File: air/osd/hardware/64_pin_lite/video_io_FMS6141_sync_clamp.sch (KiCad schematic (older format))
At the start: 30 parts, among them U10 FMS6141, U11 DAC084S085, U12 ADG704, U13 OPA830, U8 MCP6562, U9 TLV3501

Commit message: osd tidying and added reset to header connector
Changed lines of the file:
@@
-EESchema Schematic File Version 2  date Sat 29 Nov 2014 10:43:44 GMT
+EESchema Schematic File Version 2  date Sun 30 Nov 2014 15:34:12 GMT
 LIBS:power
 LIBS:device
@@
 Sheet 8 8
 Title ""
-Date "29 nov 2014"
+Date "30 nov 2014"
 Rev ""
 Comp ""
@@
 	2200 4700 2200 4600
 Wire Wire Line
-	2550 2850 2550 2050
-Wire Wire Line
-	1300 2850 2550 2850
+	2550 2050 2550 2850
+Wire Wire Line
+	2550 2850 1300 2850
 Wire Wire Line
 	2550 1150 2550 950
@@
 	7250 6250 7250 5950
 Wire Wire Line
-	6650 6250 6650 5950
+	6650 5950 6650 6250
 Connection ~ 9600 6250
 Wire Wire Line
@@
 	2200 3600 2200 3500
 Wire Wire Line
-	3200 4500 4250 4500
+	4250 4500 3200 4500
 Wire Wire Line
 	8000 4500 4750 4500
@@
 Connection ~ 9900 1600
 Wire Wire Line
-	9900 2400 9900 1600
+	9900 1600 9900 2400
 Wire Wire Line
 	9900 2400 9600 2400
@@
 	8700 1600 8700 1500
 Wire Wire Line
-	8800 1700 8800 2400
+	8800 2400 8800 1700
 Wire Wire Line
 	1250 1600 1500 1600
@@
 	1550 6050 1550 5050
 Wire Wire Line
-	6250 1200 6650 1200
+	6650 1200 6250 1200
 Connection ~ 3950 7350
 Wire Wire Line
 	3950 7450 3950 7350
 Wire Wire Line
-	4200 7350 4200 7200
+	4200 7200 4200 7350
 Wire Wire Line
 	4200 7350 3650 7350
@@
 	4600 6550 3900 6550
 Wire Wire Line
-	3900 6200 3900 6550
+	3900 6550 3900 6200
 Wire Wire Line
 	1550 5050 5850 5050
@@
 	4800 1000 4800 1200
 Wire Wire Line
-	3300 700  6100 700
+	6100 700  3300 700
 Wire Wire Line
 	6650 1400 6400 1400
@@
 	7350 3700 8000 3700
 Wire Wire Line
-	1300 3100 3300 3100
+	3300 3100 1300 3100
 Wire Wire Line
 	6550 1600 6550 2050
@@
 	5850 5050 5850 2450
 Wire Wire Line
-	1300 6350 1850 6350
-Wire Wire Line
-	1300 3100 1300 6350
+	1850 6350 1300 6350
+Wire Wire Line
+	1300 6350 1300 3100
 Wire Wire Line
 	3050 6200 2850 6200
@@
 	4200 6700 4200 6050
 Wire Wire Line
-	3550 6200 3900 6200
+	3900 6200 3550 6200
 Wire Wire Line
 	4400 6250 4400 5550
@@
 	8850 1500 8600 1500
 Wire Wire Line
-	8700 2400 8700 2100
-Wire Wire Line
-	9100 2400 8700 2400
+	8700 2100 8700 2400
+Wire Wire Line
+	8700 2400 9100 2400
 Connection ~ 8800 2400
 Wire Wire Line
@@
 	2400 4700 2400 4500
 Wire Wire Line
-	3200 3900 3200 4500
+	3200 4500 3200 3900
 Connection ~ 3200 4100
 Wire Wire Line

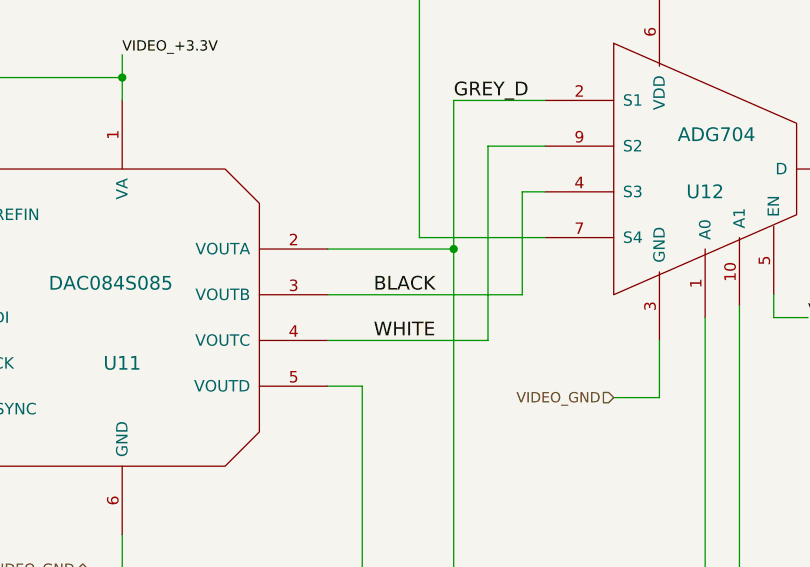
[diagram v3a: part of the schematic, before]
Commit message: added resistors to output port on board and satrted on boardtype 4 port but currently in transition
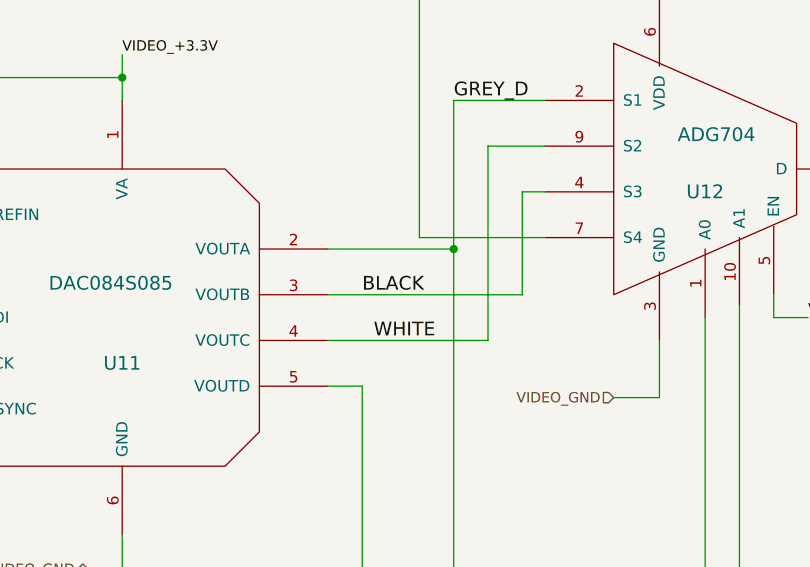
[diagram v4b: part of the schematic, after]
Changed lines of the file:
@@
-EESchema Schematic File Version 2  date Mon 01 Dec 2014 08:28:41 GMT
+EESchema Schematic File Version 2  date Tue 02 Dec 2014 12:33:05 GMT
 LIBS:power
 LIBS:device
@@
 Sheet 8 8
 Title ""
-Date "1 dec 2014"
+Date "2 dec 2014"
 Rev ""
 Comp ""
@@
 Text HLabel 8000 3500 2    60   Input ~ 0
 N_BLACK_PX
-Text Label 5900 2050 0    60   ~ 0
+Text Label 5850 2050 0    60   ~ 0
 BLACK
 Text Label 5900 2250 0    60   ~ 0

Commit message: on pcb added battery level resistor divider. On code compiled and built ok but not uploaded or tested
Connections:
- net BLACK: now also U11.4 (VOUTC), U12.9 (S2); no longer U11.3 (VOUTB), U12.4 (S3)
- net WHITE: now also U11.3 (VOUTB), U12.4 (S3); no longer U11.4 (VOUTC), U12.9 (S2)
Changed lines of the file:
@@
-EESchema Schematic File Version 2  date Tue 02 Dec 2014 12:33:05 GMT
+EESchema Schematic File Version 2  date Wed 03 Dec 2014 09:37:23 GMT
 LIBS:power
 LIBS:device
@@
 Sheet 8 8
 Title ""
-Date "2 dec 2014"
+Date "3 dec 2014"
 Rev ""
 Comp ""
@@
 Text HLabel 8000 3500 2    60   Input ~ 0
 N_BLACK_PX
-Text Label 5850 2050 0    60   ~ 0
+Text Label 5900 2250 0    60   ~ 0
 BLACK
-Text Label 5900 2250 0    60   ~ 0
+Text Label 5900 2050 0    60   ~ 0
 WHITE
 $Comp

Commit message: sasve before moving psu caps on osd
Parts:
- added P10, P9: CONN_1, symbol CONN_1
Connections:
- net at C27.1, R13.1, U8.6 (-): now also P9.1
- net at R18.1, R19.2, U8.7: now also P10.1
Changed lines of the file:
@@
-EESchema Schematic File Version 2  date Wed 03 Dec 2014 09:37:23 GMT
+EESchema Schematic File Version 2  date Sun 07 Dec 2014 14:25:55 GMT
 LIBS:power
 LIBS:device
@@
 Sheet 8 8
 Title ""
-Date "3 dec 2014"
+Date "7 dec 2014"
 Rev ""
 Comp ""
@@
 Comment4 ""
 $EndDescr
+Connection ~ 5700 5900
+Wire Wire Line
+	5850 5900 5700 5900
 Wire Wire Line
 	5700 2250 6400 2250
@@
 	2900 4100 3200 4100
 Wire Wire Line
-	5800 6400 5600 6400
+	5600 6400 5800 6400
 Connection ~ 9900 1600
 Wire Wire Line
@@
 	8800 2400 8800 1700
 Wire Wire Line
-	1250 1600 1500 1600
+	1500 1600 1250 1600
 Connection ~ 3300 1600
 Wire Wire Line
@@
 Connection ~ 4200 6250
 Wire Wire Line
-	4600 6250 4200 6250
+	4200 6250 4600 6250
 Wire Wire Line
 	4600 6550 3900 6550
@@
 	1550 5050 5850 5050
 Wire Wire Line
-	6400 6400 6300 6400
+	6700 6400 6300 6400
 Wire Wire Line
 	8000 3500 7500 3500
@@
 	3650 2350 3850 2350
 Wire Wire Line
-	4800 1000 4800 1200
+	4800 1200 4800 1000
 Wire Wire Line
 	6100 700  3300 700
@@
 Connection ~ 3650 6200
 Wire Wire Line
-	4200 6700 4200 6050
+	4200 6050 4200 6700
 Wire Wire Line
 	3900 6200 3550 6200
@@
 Connection ~ 4400 6250
 Wire Wire Line
-	8850 1500 8600 1500
+	8600 1500 8850 1500
 Wire Wire Line
 	8700 2100 8700 2400
@@
 	1350 2400 1350 2850
 Wire Wire Line
-	9850 1600 9950 1600
+	9950 1600 9850 1600
 Wire Wire Line
 	1750 4250 1300 4250
@@
 Wire Wire Line
 	6550 2050 5700 2050
+Wire Wire Line
+	3800 6200 3800 5950
+Connection ~ 3800 6200
+$Comp
+L CONN_1 P10
+U 1 1 5482DEBF
+P 6000 5900
+F 0 "P10" H 6080 5900 40  0000 L CNN
+F 1 "CONN_1" H 6000 5955 30  0001 C CNN
+	1    6000 5900
+	1    0    0    -1
+$EndComp
+$Comp
+L CONN_1 P9
+U 1 1 5482DEA0
+P 3800 5800
+F 0 "P9" H 3880 5800 40  0000 L CNN
+F 1 "CONN_1" H 3800 5855 30  0001 C CNN
+	1    3800 5800
+	0    -1   -1   0
+$EndComp
 Text HLabel 8250 5450 0    45   Input ~ 0
 VIDEO_+3.3V
@@
 Text HLabel 1250 1600 0    60   Input ~ 0
 VIDEO_IN
-Text HLabel 6400 6400 2    60   Output ~ 0
+Text HLabel 6700 6400 2    60   Output ~ 0
 CSYNC
 $Comp

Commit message: must be nearly finalised pcb ready for sending off.Disco circuit tested  so now just hope its right for pcb
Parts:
- C27: value 470pF -> 250pF
- R13: value 620R -> 1K2
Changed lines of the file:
@@
-EESchema Schematic File Version 2  date Sun 07 Dec 2014 14:25:55 GMT
+EESchema Schematic File Version 2  date Sun 07 Dec 2014 19:48:20 GMT
 LIBS:power
 LIBS:device
@@
 P 3650 6500
 F 0 "C27" H 3700 6350 50  0000 L CNN
-F 1 "470pF" H 3400 6600 50  0000 L CNN
+F 1 "250pF" H 3400 6600 50  0000 L CNN
 	1    3650 6500
 	1    0    0    -1
@@
 P 3300 6200
 F 0 "R13" V 3380 6200 50  0000 C CNN
-F 1 "620R" V 3300 6200 50  0000 C CNN
+F 1 "1K2" V 3300 6200 50  0000 C CNN
 	1    3300 6200
 	0    1    1    0
